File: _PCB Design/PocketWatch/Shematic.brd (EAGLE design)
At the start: 160 x 100 mm, 55 parts, among them U2 ATTINY88-AU

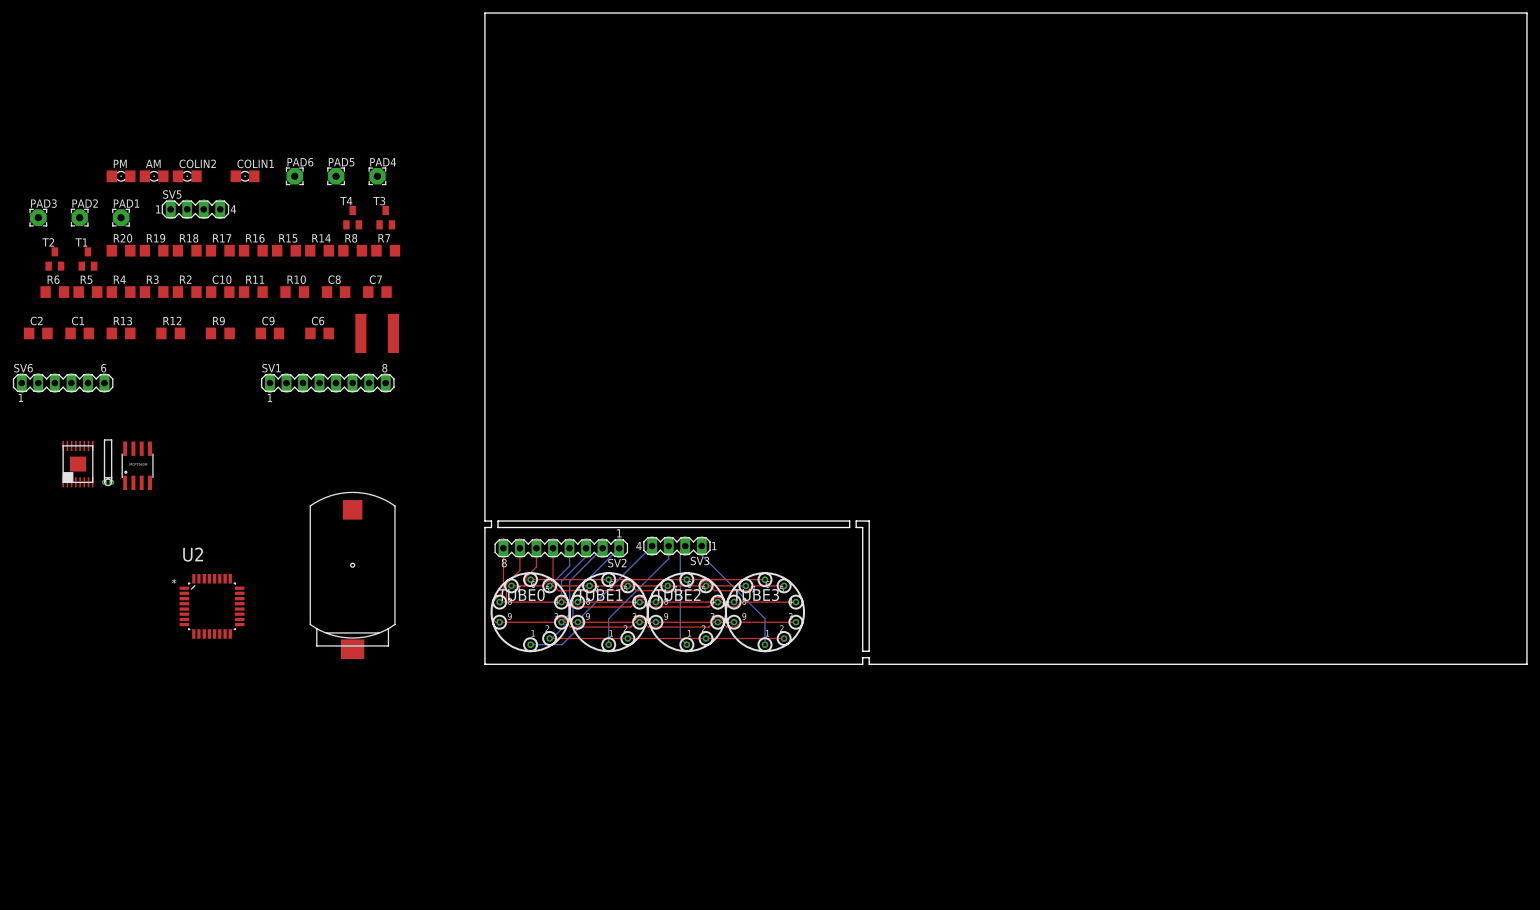
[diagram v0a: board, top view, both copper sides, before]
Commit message: Begin placement of main board. Swapped LEDs for through hole
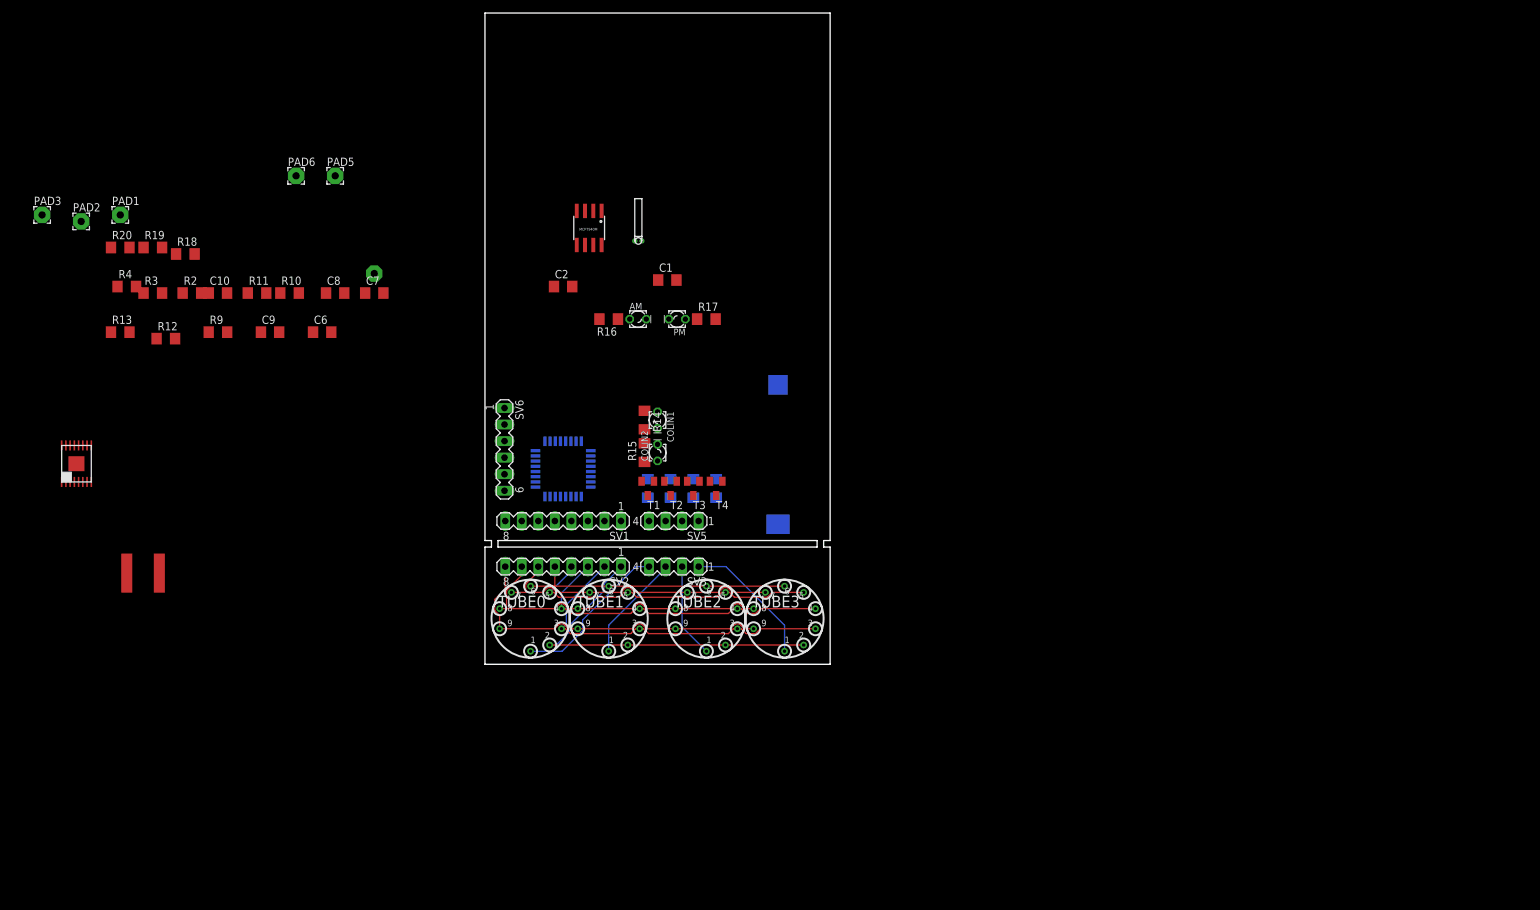
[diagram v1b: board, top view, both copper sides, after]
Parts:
- AM, COLIN1, COLIN2, PM: device eagle-ltspice:LED_1206 -> eagle-ltspice:LED_LD260
- R5, R6, R7, R8: value 30 -> 1k
- moved T2 100.9 mm to (28.5, 27.0), turned to 180 degrees
- moved R6 99.2 mm to (28.5, 27.0), flipped to the bottom, turned to 270 degrees
- moved T1 92.9 mm to (25.0, 27.0), turned to 180 degrees
- moved R5 91.1 mm to (25.0, 27.0), flipped to the bottom, turned to 270 degrees
- moved C1 90.6 mm to (28.0, 59.0)
- moved 6PF 89.5 mm to (23.0, 65.0)
- moved PM 88.2 mm to (29.5, 53.0), turned to 180 degrees
- moved SV5 87.7 mm to (29.0, 22.0), turned to 180 degrees
- moved COLIN2 83.8 mm to (26.5, 32.5), turned to 90 degrees
- moved C2 80.9 mm to (12.0, 58.0)
- moved MCP7940M 78.4 mm to (16.0, 67.0), turned to 180 degrees
- moved AM 77.5 mm to (23.5, 53.0)
- moved R17 75.4 mm to (34.0, 53.0)
- moved COLIN1 73.6 mm to (26.5, 37.5), turned to 270 degrees
- moved T4 69.6 mm to (35.5, 27.0), turned to 180 degrees
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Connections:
- net GND: now also AM.K, COLIN1.K, COLIN2.K, PM.K; no longer AM.C, COLIN1.C, COLIN2.C, PM.C
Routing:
- net TG1_2: track 19.0 -> 16.6 mm
- net TG3_2: track 19.2 -> 20.9 mm
- net SEG_DOT_2: track 54.5 -> 56.2 mm
- net TG2_2: track 15.9 -> 14.5 mm
- net SEG_C_2: track 47.7 -> 49.0 mm
- net SEG_B_2: track 51.8 -> 53.1 mm
- net SEG_A_2: track 44.9 -> 46.2 mm
- net SEG_G_2: track 44.4 -> 45.6 mm
- net SEG_F_2: track 41.0 -> 42.3 mm
- net TG0_2: track 25.7 -> 24.5 mm
- net SEG_D_2: track 47.1 -> 48.3 mm
- net SEG_E_2: track 50.8 -> 51.4 mm
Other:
- board size 160 x 100 mm -> 53 x 100 mm

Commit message: Re-routed tube board with thicker traces. Improved 3rd party board dimension accuracy.
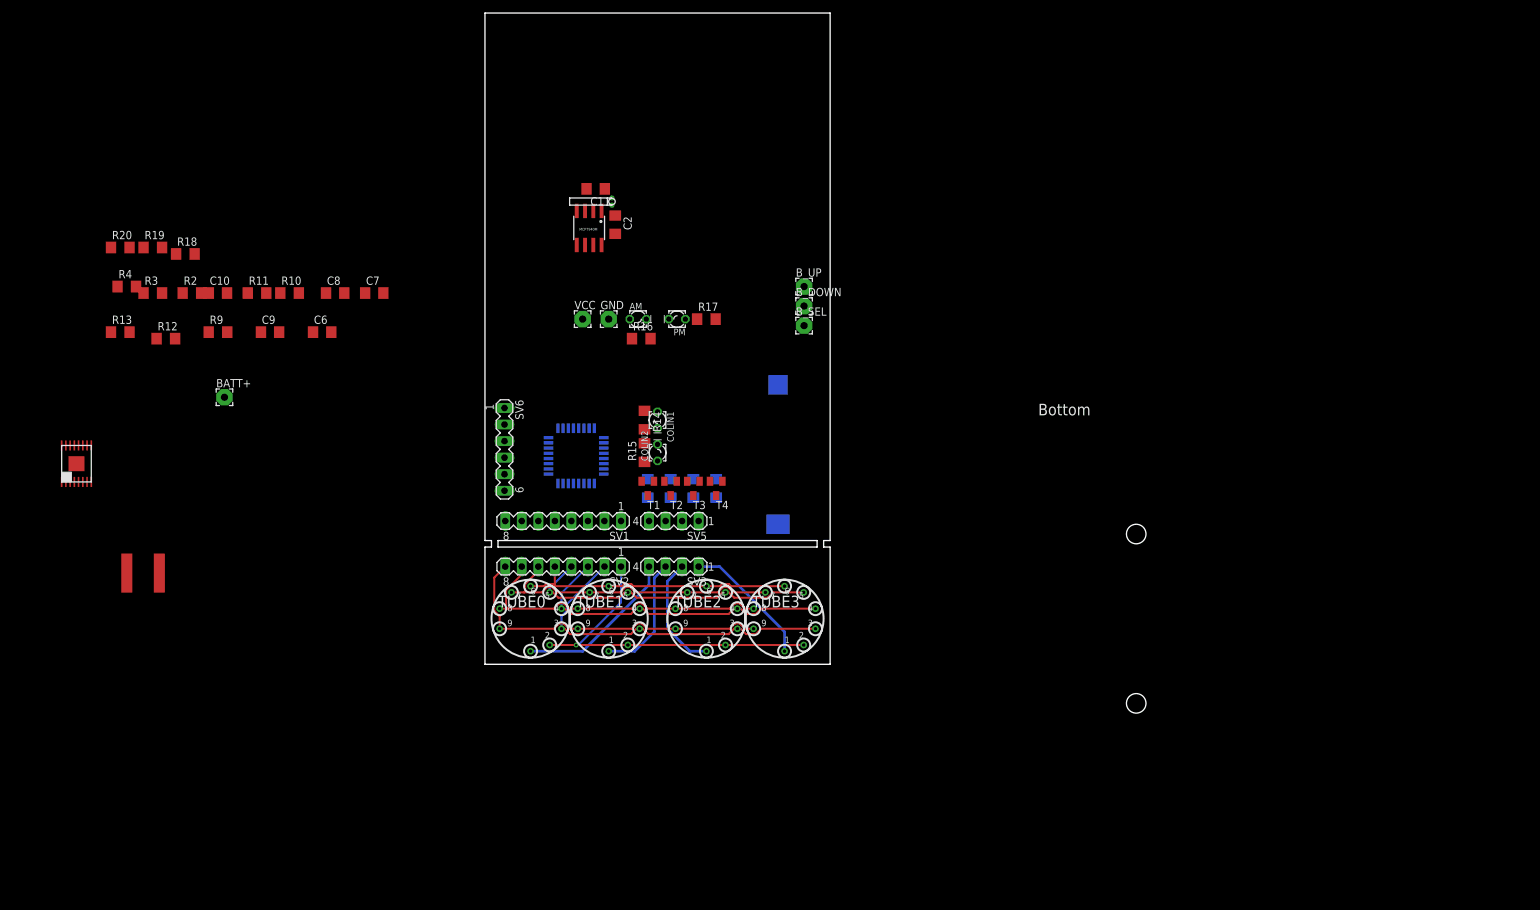
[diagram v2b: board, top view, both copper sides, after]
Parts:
- removed PAD1, PAD2, PAD3: WIREPAD2,54/1,1, wirepad:2,54/1,1
- removed PAD4, PAD5, PAD6: WIREPAD, wirepad:2,54/1,1
- added BATT+, GND, VCC: WIREPAD2,54/1,1, wirepad:2,54/1,1
- added B_DOWN, B_SEL, B_UP: WIREPAD, wirepad:2,54/1,1
- moved C1 17.8 mm to (17.0, 73.0), turned to 180 degrees
- moved C2 12.4 mm to (20.0, 67.5), turned to 270 degrees
- moved 6PF 6.52 mm to (19.5, 70.5), turned to 90 degrees
- moved R16 5.83 mm to (24.0, 50.0), turned to 0 degrees
- moved U2 2.83 mm to (14.0, 32.0)
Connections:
- net BATT+: now also BATT+.1; no longer PAD1.1
- net B_DOWN: now also B_DOWN.1; no longer PAD6.1
- net B_SEL: now also B_SEL.1; no longer PAD4.1
- net B_UP: now also B_UP.1; no longer PAD5.1
- net GND: now also GND.1; no longer PAD3.1
- net VCC: now also VCC.1; no longer PAD2.1
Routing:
- net TG2_2: track 14.5 -> 17.9 mm
- net TG1_2: track 16.6 -> 19.0 mm
- net SEG_DOT_2: track 56.2 -> 54.1 mm, vias 0 -> 1
- net TG0_2: track 24.5 -> 25.2 mm
- net TG3_2: track 20.9 -> 20.3 mm
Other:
- board text added: "Bottom"
- board text added: "Top"

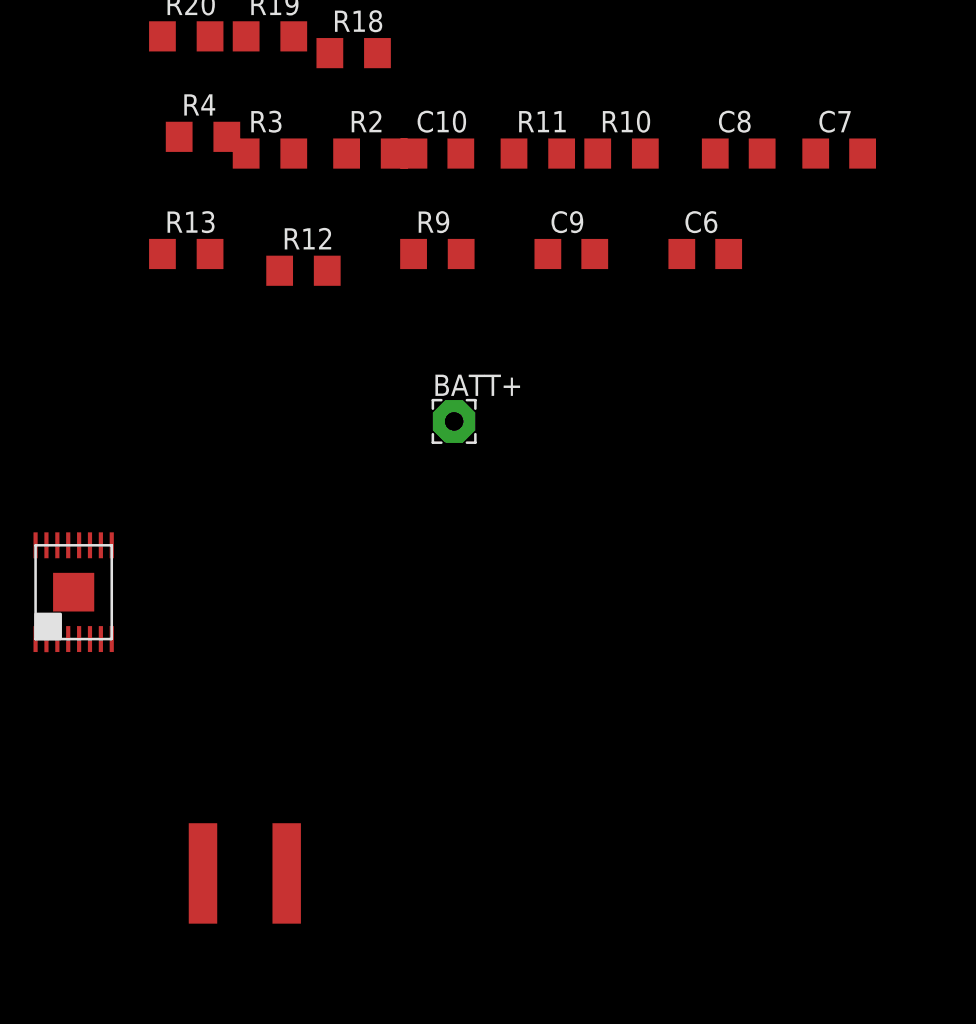
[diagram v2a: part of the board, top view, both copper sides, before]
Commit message: Removed 1st party boost converter.
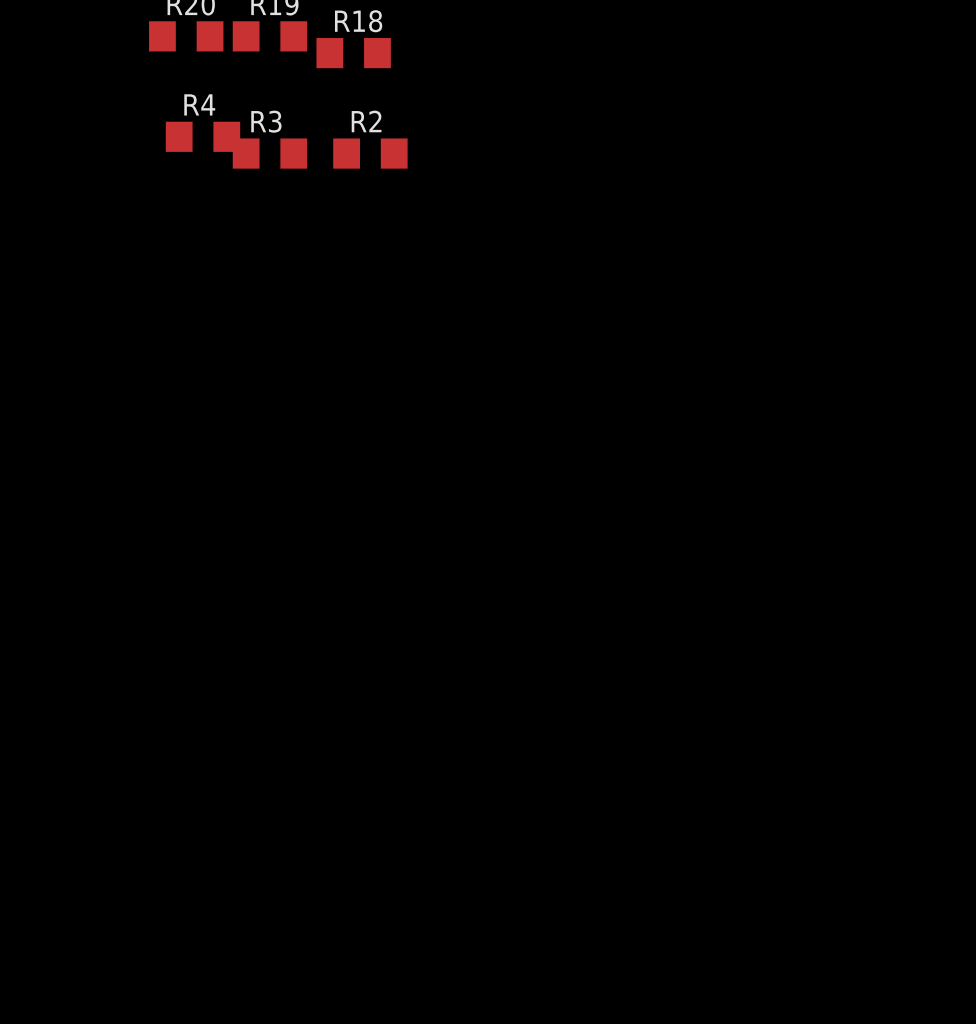
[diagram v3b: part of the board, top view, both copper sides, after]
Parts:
- removed BATT+: WIREPAD2,54/1,1, wirepad:2,54/1,1
- removed C10: 1uF, eagle-ltspice:C1206
- removed C6: 100nF, eagle-ltspice:C1206
- removed C7: 10uF, eagle-ltspice:C1206
- removed C8: 10pF, eagle-ltspice:C1206
- removed C9: 220uF, eagle-ltspice:C1206
- removed LLC_ASPI-6045S: 4.30uH, Library:LLC_ASPI-6045S
- removed R10: 396k, eagle-ltspice:R1206
- removed R11: 182k, eagle-ltspice:R1206
- removed R12: 1.62M, eagle-ltspice:R1206
- removed R13, R9: 1.96M, eagle-ltspice:R1206
- removed U$6: TPS61030, Library:TPS61030
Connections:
- removed net BATT+: BATT+.1, C6.1, C7.1, LLC_ASPI-6045S.P$1, R9.2, U$6.6, U$6.9
- removed net N$10: R13.1, U$6.10
- removed net N$11: R10.2, R9.1, U$6.7
- removed net N$13: C8.2, R11.2, R12.1, U$6.12
- removed net N$8: LLC_ASPI-6045S.P$2, U$6.1, U$6.2
- net GND: no longer C10.2, C6.2, C7.2, C9.2, R10.1, R11.1, U$6.11, U$6.16, U$6.17, U$6.3, U$6.4, U$6.5, U$6.8
- net VCC: no longer C10.1, C8.1, C9.1, R12.2, R13.2, U$6.13, U$6.15, U$6.P$14

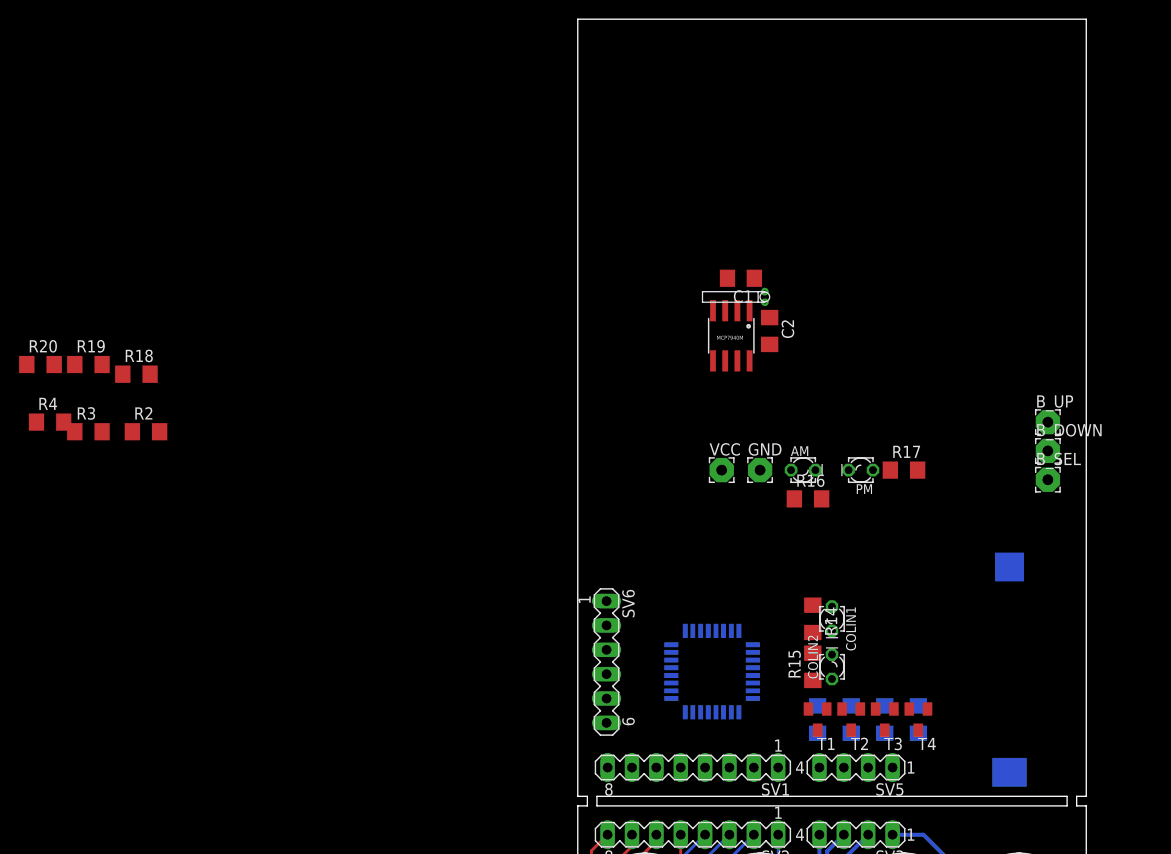
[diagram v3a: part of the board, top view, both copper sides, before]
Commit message: Began routing main board. Modified component placement
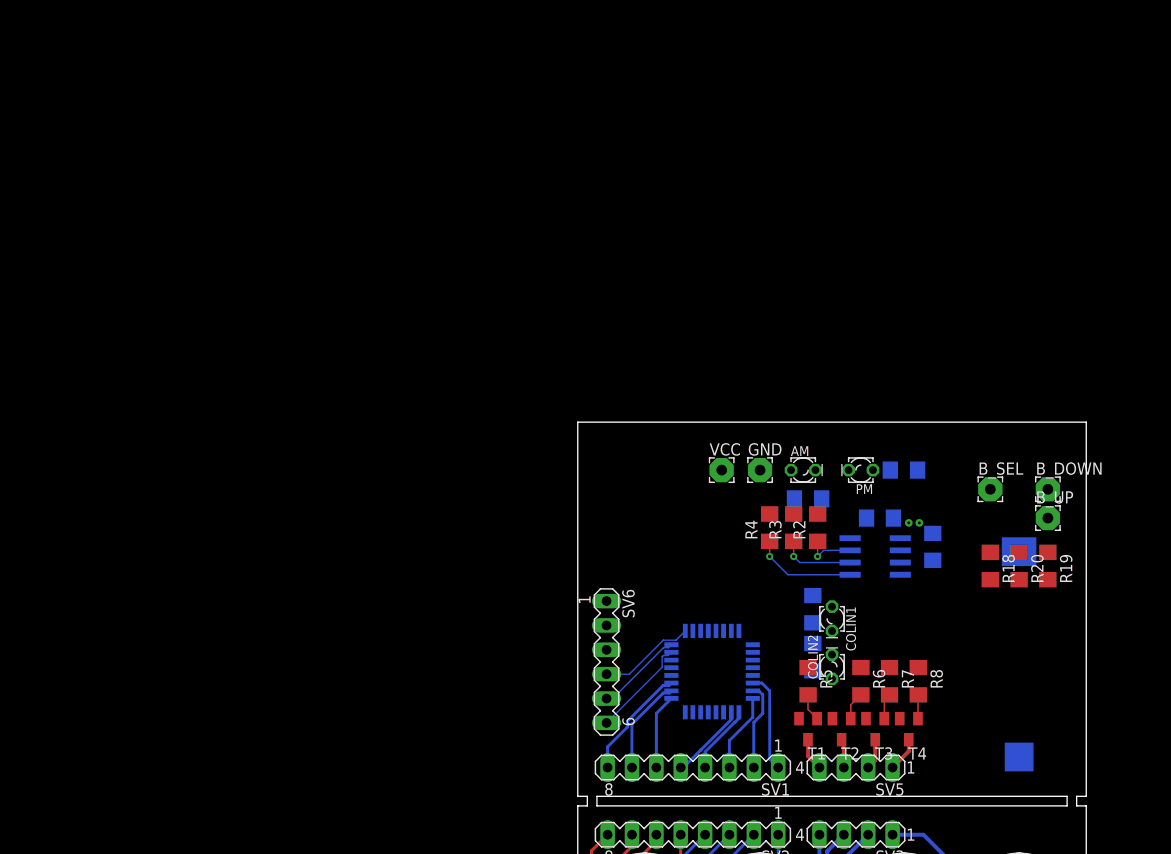
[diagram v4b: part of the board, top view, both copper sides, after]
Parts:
- moved R20 104.1 mm to (46.0, 43.0), turned to 270 degrees
- moved R19 102.2 mm to (49.0, 43.0), turned to 270 degrees
- moved R18 91.2 mm to (43.0, 43.0), turned to 270 degrees
- moved R4 75.8 mm to (20.0, 47.0), turned to 90 degrees
- moved R3 74.2 mm to (22.5, 47.0), turned to 90 degrees
- moved R2 70.7 mm to (25.0, 47.0), turned to 90 degrees
- moved C1 34.4 mm to (37.0, 45.0), flipped to the bottom, turned to 270 degrees
- moved 6PF 27.5 mm to (34.5, 47.5), flipped to the bottom, turned to 180 degrees
- moved MCP7940M 27.5 mm to (31.0, 44.0), flipped to the bottom, turned to 270 degrees
- moved C2 22.6 mm to (31.5, 48.0), flipped to the bottom, turned to 0 degrees
- moved U$5 20.0 mm to (46.0, 43.0), turned to 180 degrees
- moved B_UP 10.0 mm to (49.0, 48.0)
- moved B_SEL 6.08 mm to (43.0, 51.0)
- moved R5 4.12 mm to (24.0, 31.0), flipped to the top
- moved R6 4.12 mm to (29.5, 31.0), flipped to the top
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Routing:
- net SEG_G: track 0.00 -> 11.9 mm
- net SDA: track 0.00 -> 10.8 mm, vias 0 -> 1
- net SEG_DOT: track 0.00 -> 10.5 mm
- net MOSI: track 0.00 -> 10.4 mm
- net SCK: track 0.00 -> 10.1 mm
- net SEG_F: track 0.00 -> 10.1 mm
- net SEG_A: track 0.00 -> 9.18 mm
- net MISO: track 0.00 -> 9.08 mm
- net SEG_B: track 0.00 -> 8.21 mm
- net SEG_D: track 0.00 -> 8.10 mm
- net SEG_E: track 0.00 -> 7.86 mm
- net SCL: track 0.00 -> 7.72 mm, vias 0 -> 1
- net SEG_C: track 0.00 -> 7.23 mm
- net MFP: track 0.00 -> 5.22 mm, vias 0 -> 1
- net TG3: track 0.00 -> 3.60 mm
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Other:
- board size 53 x 100 mm -> 53 x 58 mm
